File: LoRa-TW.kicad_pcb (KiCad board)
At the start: 2 copper layers, 4 parts, among them U1 SX1262IMLTRT

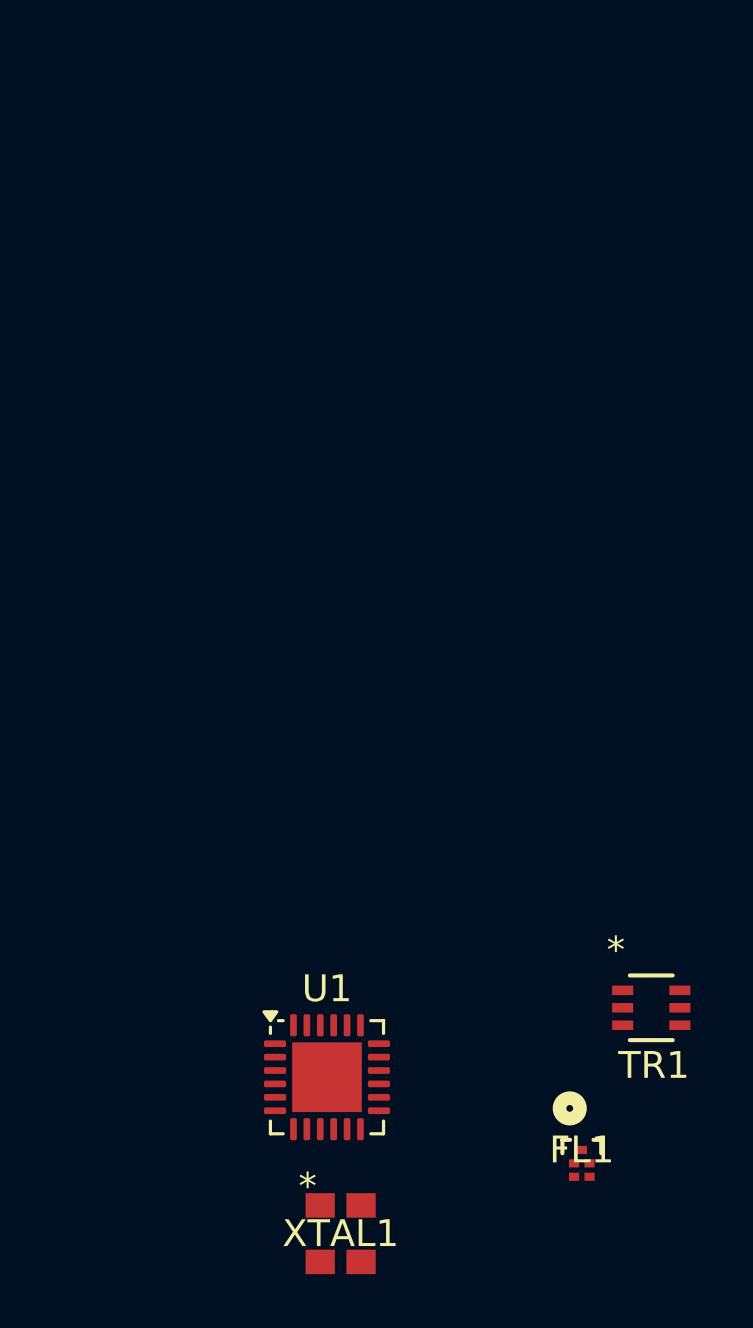
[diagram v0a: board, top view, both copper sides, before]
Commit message: update receive of schematic
- update symbol
- place rx path components
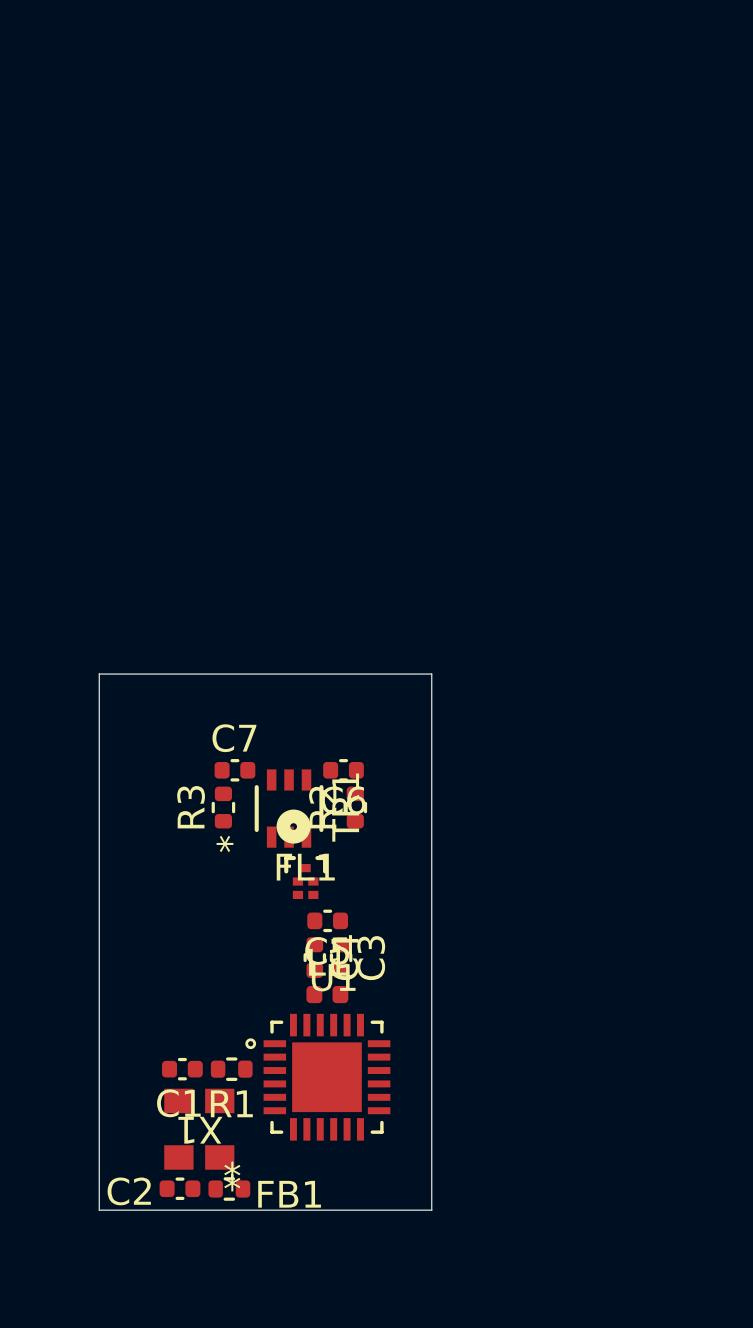
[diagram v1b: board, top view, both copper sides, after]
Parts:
- removed XTAL1: NT2016SA-32MHz-END4263A, LoRa-TW:NT2016SA_NDK
- added C1: 10P, Capacitor_SMD:C_0402_1005Metric, F.Cu at (149.4, 125.6)
- added C2: 100n, Capacitor_SMD:C_0402_1005Metric, F.Cu at (149.4, 130.0)
- added C3: 1p8, Capacitor_SMD:C_0402_1005Metric, F.Cu at (155.4, 121.4)
- added C4: 2p4, Capacitor_SMD:C_0402_1005Metric, F.Cu at (154.4, 121.4)
- added C5: 2p4, Capacitor_SMD:C_0402_1005Metric, F.Cu at (154.9, 120.0)
- added C6: 1n, Capacitor_SMD:C_0402_1005Metric, F.Cu at (155.5, 114.4)
- added C7: 1n, Capacitor_SMD:C_0402_1005Metric, F.Cu at (151.4, 114.4)
- added FB1: 100K, Resistor_SMD:R_0402_1005Metric, F.Cu at (151.2, 130.0)
- added L1: 15n, Inductor_SMD:L_0402_1005Metric, F.Cu at (154.9, 122.8)
- added R1: 220, Resistor_SMD:R_0402_1005Metric, F.Cu at (151.3, 125.6)
- added R2: 100, Resistor_SMD:R_0402_1005Metric, F.Cu at (155.9, 115.8)
- added R3: 100, Resistor_SMD:R_0402_1005Metric, F.Cu at (151.0, 115.8)
- added X1: TCXO, 32MHz, 2.0x1.6mm, LoRa-TW:NT2016SA_NDK, F.Cu at (150.1, 127.8)
- U1: footprint Package_DFN_QFN:QFN-24-1EP_4x4mm_P0.5mm_EP2.6x2.6mm -> LoRa-TW:SX1262IMLTRT
- moved TR1 15.4 mm to (153.4, 115.8), turned to 90 degrees
- moved FL1 14.7 mm to (154.0, 118.6)
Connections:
- FL1 pad 1: unconnected-(FL1-IN-Pad1) -> Net-(FL1-IN)
- FL1 pad 2: unconnected-(FL1-GND-Pad2) -> GND
- FL1 pad 3: unconnected-(FL1-GND-Pad3) -> GND
- FL1 pad 4: unconnected-(FL1-OUT-Pad4) -> Net-(FL1-OUT)
- FL1 pad 5: unconnected-(FL1-GND-Pad5) -> GND
- TR1 pad 3: unconnected-(TR1-RF2-Pad3) -> Net-(FL1-IN)
- TR1 pad 4: unconnected-(TR1-CTRL-Pad4) -> Net-(TR1-CTRL)
- TR1 pad 6: unconnected-(TR1-*CTRL/VDD-Pad6) -> Net-(TR1-~{CTRL}/VDD)
- U1 pad 12: unconnected-(U1-DIO2-Pad12) -> /DIO2
- U1 pad 15: unconnected-(U1-~{RESET}-Pad15) -> /~{RESET}
- U1 pad 21: unconnected-(U1-RFI_P-Pad21) -> Net-(U1-RFI_P)
- U1 pad 22: unconnected-(U1-RFI_N-Pad22) -> Net-(U1-RFI_N)
- U1 pad 3: unconnected-(U1-XTA-Pad3) -> /CLK_{32M}
- U1 pad 6: unconnected-(U1-DIO3-Pad6) -> /DIO3_CLK_{EN}
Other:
- board outline added: 12.4 x 20 mm

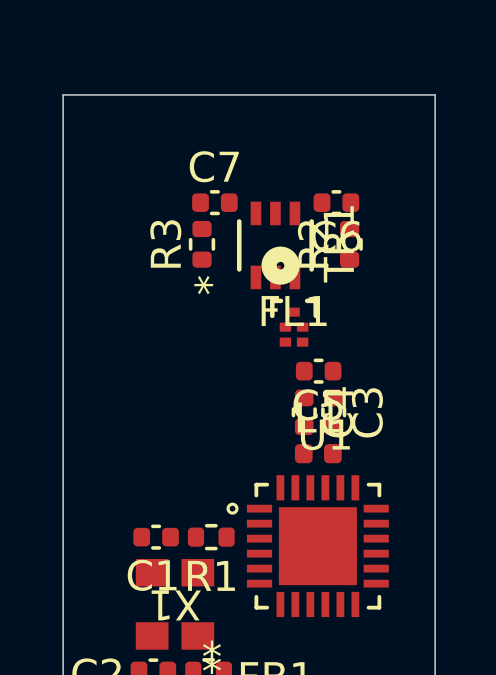
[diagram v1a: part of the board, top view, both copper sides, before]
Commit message: update transmit of schematic
- update TX path
- correct some components properties
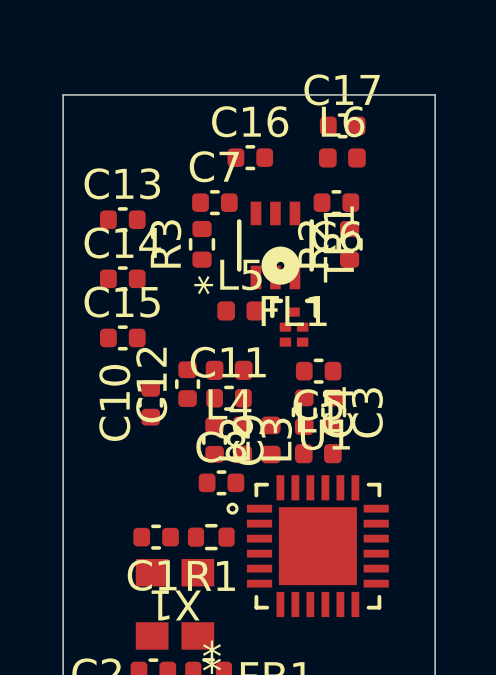
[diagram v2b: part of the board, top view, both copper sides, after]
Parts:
- added C10: 3p0, Capacitor_SMD:C_0402_1005Metric, F.Cu at (149.3, 121.1)
- added C11: 3p0, Capacitor_SMD:C_0402_1005Metric, F.Cu at (151.9, 120.9)
- added C12: 5p6, Capacitor_SMD:C_0402_1005Metric, F.Cu at (150.5, 120.5)
- added C13: 39p, Capacitor_SMD:C_0402_1005Metric, F.Cu at (148.3, 115.0)
- added C14: 1p8, Capacitor_SMD:C_0402_1005Metric, F.Cu at (148.3, 117.0)
- added C15: 39p, Capacitor_SMD:C_0402_1005Metric, F.Cu at (148.3, 118.9)
- added C16: 3p3, Capacitor_SMD:C_0402_1005Metric, F.Cu at (152.6, 112.9)
- added C17: 3p3, Capacitor_SMD:C_0402_1005Metric, F.Cu at (155.7, 111.8)
- added C8: 47n, Capacitor_SMD:C_0402_1005Metric, F.Cu at (151.6, 123.8)
- added C9: 47p, Capacitor_SMD:C_0402_1005Metric, F.Cu at (151.4, 122.3)
- added L2: 0, Inductor_SMD:L_0402_1005Metric, F.Cu at (153.3, 122.3)
- added L3: 47n, Inductor_SMD:L_0402_1005Metric, F.Cu at (152.3, 122.3)
- added L4: 2n5, Inductor_SMD:L_0402_1005Metric, F.Cu at (151.9, 120.0)
- added L5: 4n7, Inductor_SMD:L_0402_1005Metric, F.Cu at (152.3, 118.0)
- added L6: 9n1, Inductor_SMD:L_0402_1005Metric, F.Cu at (155.7, 112.9)
- FB1: value 100K -> 10R@100MHz
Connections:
- net /DIO2 renamed /DIO2_ANT_{SW}
- L1 pad 1: Net-(U1-RFI_N) -> Net-(U1-RFI_P)
- L1 pad 2: Net-(U1-RFI_P) -> Net-(U1-RFI_N)
- TR1 pad 1: unconnected-(TR1-RF1-Pad1) -> Net-(TR1-RF1)
- TR1 pad 2: unconnected-(TR1-GND-Pad2) -> GND
- TR1 pad 5: unconnected-(TR1-RFC-Pad5) -> Net-(TR1-RFC)
- U1 pad 13: unconnected-(U1-DIO1-Pad13) -> /DIO1_INT
- U1 pad 16: unconnected-(U1-MISO-Pad16) -> /SPI_MISO
- U1 pad 17: unconnected-(U1-MOSI-Pad17) -> /SPI_MOSI
- U1 pad 18: unconnected-(U1-SCK-Pad18) -> /SPI_CLK
- U1 pad 19: unconnected-(U1-NSS-Pad19) -> /SPI_NSS
- U1 pad 23: unconnected-(U1-RFO-Pad23) -> Net-(U1-RFO)
- U1 pad 24: unconnected-(U1-VR_PA-Pad24) -> Net-(U1-VR_PA)

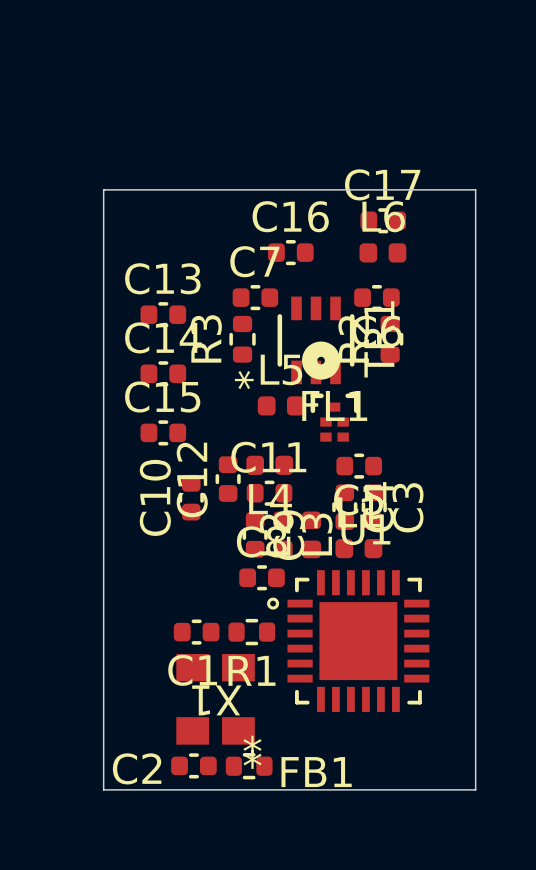
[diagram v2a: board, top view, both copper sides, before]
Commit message: update schematic for power input
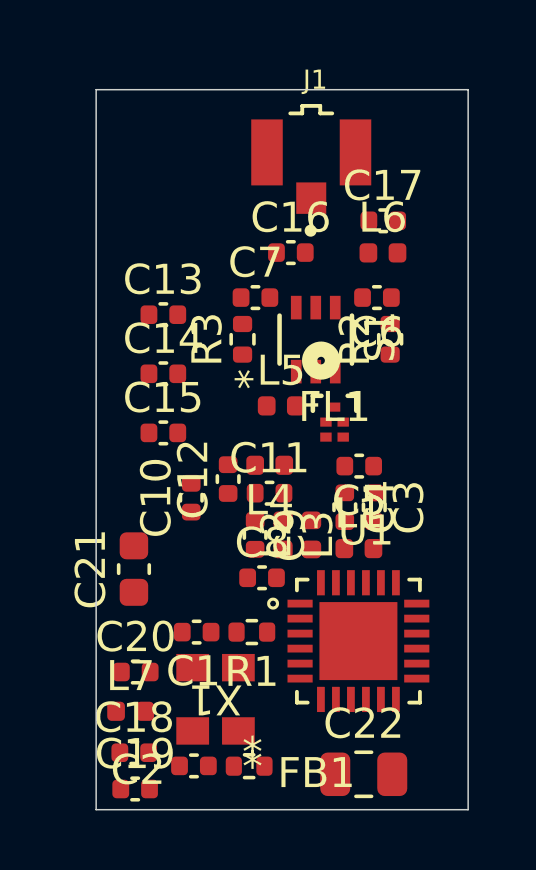
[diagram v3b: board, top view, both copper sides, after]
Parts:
- removed TR1: PE4259-63, LoRa-TW:SC-70-6_PSM
- added C18: 470n, Capacitor_SMD:C_0402_1005Metric, F.Cu at (147.4, 129.6)
- added C19: 100n, Capacitor_SMD:C_0402_1005Metric, F.Cu at (147.4, 130.8)
- added C20: 100n, Capacitor_SMD:C_0402_1005Metric, F.Cu at (147.4, 126.9)
- added C21: 1u, Capacitor_SMD:C_0603_1608Metric, F.Cu at (147.4, 123.5)
- added C22: 10u, Capacitor_SMD:C_0805_2012Metric, F.Cu at (155.0, 130.3)
- added J1: MHF-I/U.FL, LoRa-TW:IPEX_20279-001E-03, F.Cu at (153.3, 109.6)
- added L7: 15u, Inductor_SMD:L_0402_1005Metric, F.Cu at (147.2, 128.2)
- added S1: PE4259-63, LoRa-TW:SC-70-6_PSM, F.Cu at (153.4, 115.8)
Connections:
- U1 pad 1: unconnected-(U1-VDD_IN-Pad1) -> VDD
- U1 pad 10: unconnected-(U1-VBAT-Pad10) -> VDD
- U1 pad 11: unconnected-(U1-VBAT_IO-Pad11) -> VDD
- U1 pad 14: unconnected-(U1-BUSY-Pad14) -> /BUSY
- U1 pad 7: unconnected-(U1-VREG-Pad7) -> /VREG
- U1 pad 9: unconnected-(U1-DCC_SW-Pad9) -> Net-(U1-DCC_SW)
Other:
- board size 12.4 x 20 mm -> 12.4 x 24 mm

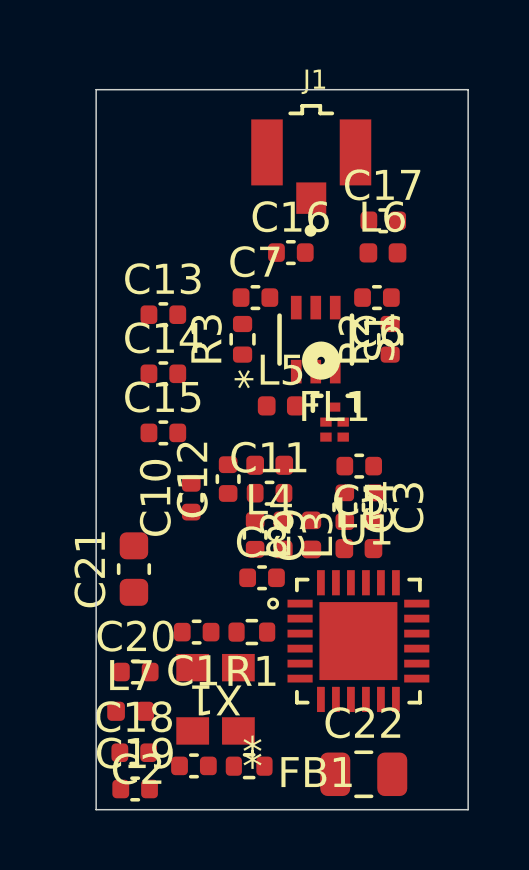
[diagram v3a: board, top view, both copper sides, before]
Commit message: update schematic & pcb for new footprint
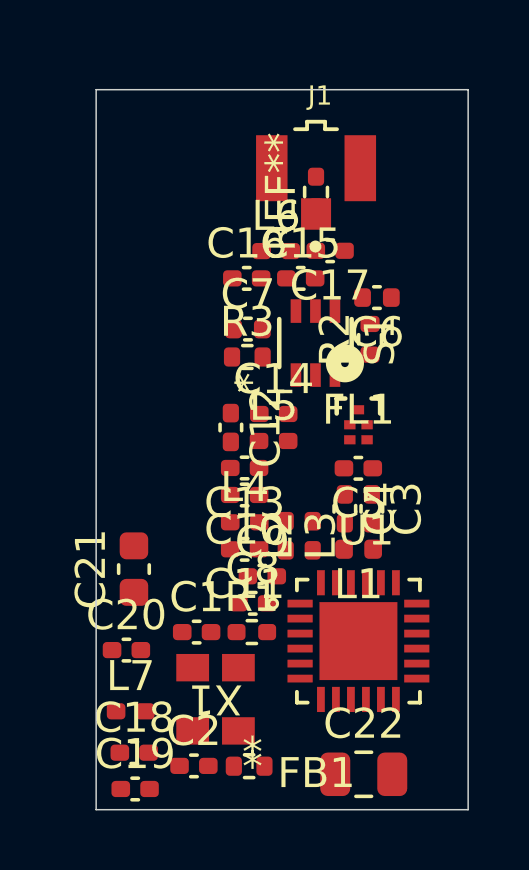
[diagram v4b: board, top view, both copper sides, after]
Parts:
- added REF**: R_HF_0402_1005Metric, LoRa-TW:R_HF_0402_1005Metric, F.Cu at (153.4, 110.9)
- C1, C10, C11, C12, C13, C14, C15, C16, C17, C18, C19, C2, C20, C3, C4, C5, C8, C9: footprint Capacitor_SMD:C_0402_1005Metric -> LoRa-TW:C_HF_0402_1005Metric
- L2, L3, L4, L5, L6, L7: footprint Inductor_SMD:L_0402_1005Metric -> LoRa-TW:L_HF_0402_1005Metric
- R1: footprint Resistor_SMD:R_0402_1005Metric -> LoRa-TW:R_HF_0402_1005Metric
- moved C15 6.89 mm to (152.9, 113.8)
- moved C13 5.78 mm to (151.1, 120.1), turned to 180 degrees
- moved C14 3.92 mm to (152.0, 118.3)
- moved L6 3.56 mm to (152.1, 112.9)
- moved L4 2.07 mm to (151.1, 121.9), turned to 0 degrees
- moved C11 2.05 mm to (151.1, 122.8), turned to 180 degrees
- moved C17 2.03 mm to (153.9, 112.8), turned to 180 degrees
- moved C10 1.78 mm to (151.1, 121.0), turned to 180 degrees
- moved C12 1.72 mm to (150.6, 118.7), turned to -90 degrees
- moved C16 1.70 mm to (151.1, 113.8)
- moved C9 1.40 mm to (151.6, 123.7), turned to 0 degrees
- moved L5 1.20 mm to (152.0, 119.2)
- moved C7 1.08 mm to (151.2, 115.5)
- moved C8 0.90 mm to (151.3, 124.6)
- moved FL1 0.80 mm to (154.8, 118.7)
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
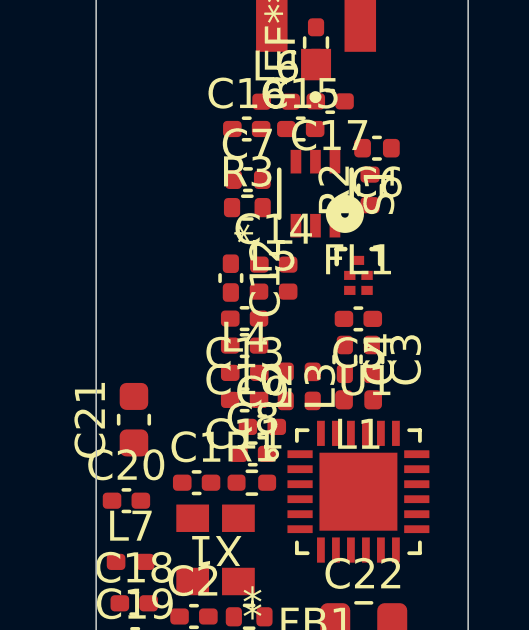
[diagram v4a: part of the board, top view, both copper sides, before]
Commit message: update SAW Filter properties with 3D Model
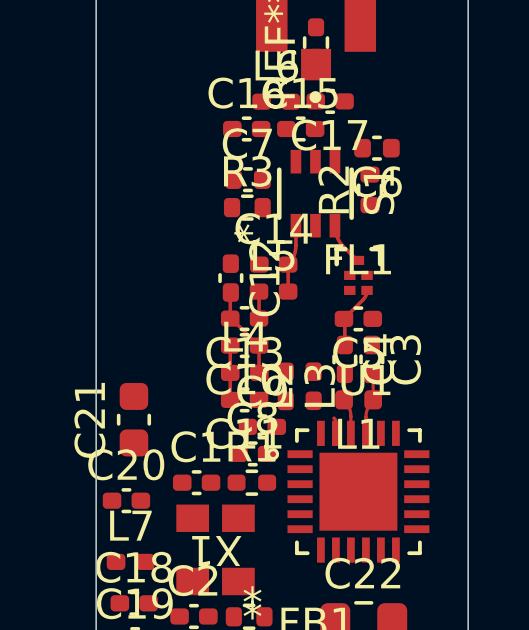
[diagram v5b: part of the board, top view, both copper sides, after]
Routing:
- net Net-(C10-Pad1): track 0.00 -> 3.14 mm
- net Net-(S1-RF1): track 0.00 -> 2.26 mm
- net Net-(FL1-OUT): track 0.00 -> 2.13 mm
- net Net-(U1-RFI_P): track 0.00 -> 2.06 mm
- net Net-(U1-RFI_N): track 0.00 -> 2.05 mm
- net Net-(C10-Pad2): track 0.00 -> 1.81 mm
- net Net-(FL1-IN): track 0.00 -> 1.45 mm
- net Net-(C13-Pad1): track 0.00 -> 0.90 mm
- net Net-(U1-RFO): track 0.00 -> 0.58 mm
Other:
- copper layers 2 -> 4

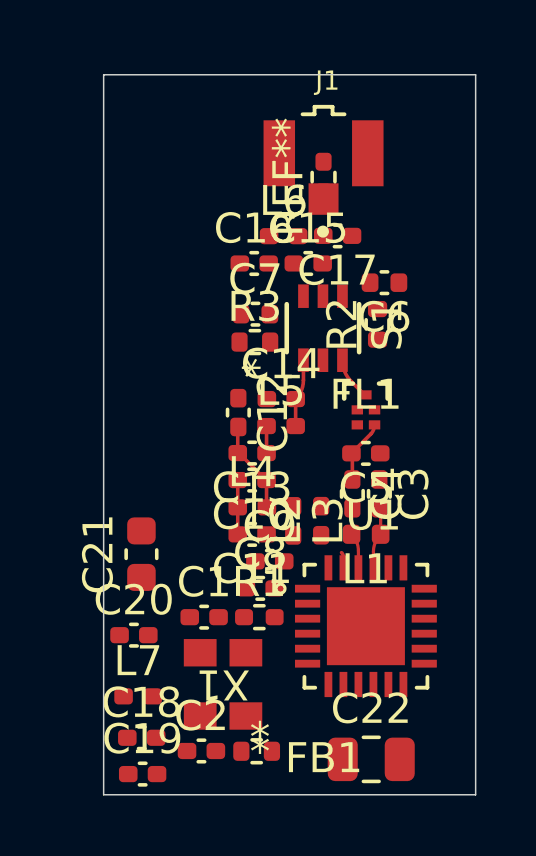
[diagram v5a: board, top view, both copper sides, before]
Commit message: update layout for RF parts
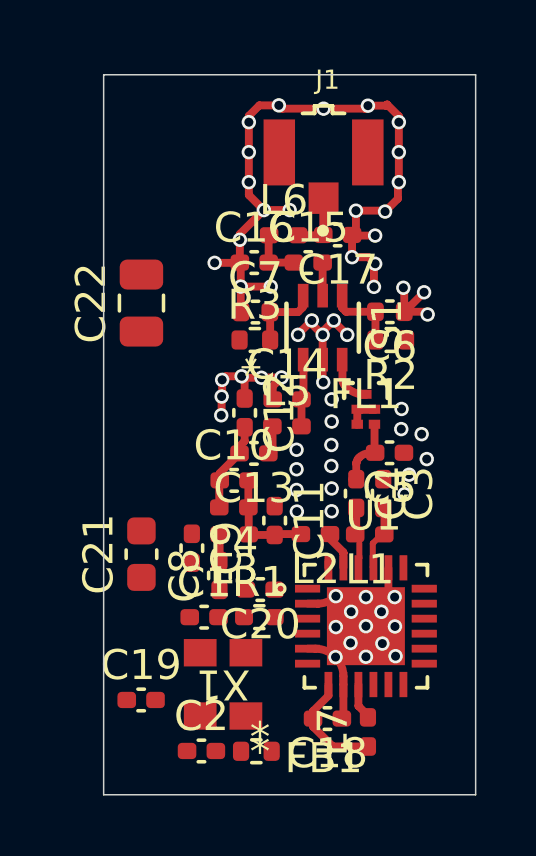
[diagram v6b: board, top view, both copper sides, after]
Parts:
- removed REF**: R_HF_0402_1005Metric, LoRa-TW:R_HF_0402_1005Metric
- L1: footprint Inductor_SMD:L_0402_1005Metric -> LoRa-TW:L_HF_0402_1005Metric
- moved C22 17.0 mm to (147.4, 115.1), turned to 90 degrees
- moved L7 7.75 mm to (154.9, 129.4), turned to 90 degrees
- moved C18 6.22 mm to (153.6, 128.9), turned to 180 degrees
- moved C20 4.48 mm to (151.3, 124.6), turned to 180 degrees
- moved C9 2.64 mm to (149.0, 123.3), turned to -90 degrees
- moved C19 2.47 mm to (147.3, 128.3)
- moved L3 2.02 mm to (150.4, 122.8), turned to 180 degrees
- moved C8 1.43 mm to (150.0, 124.2), turned to 90 degrees
- moved C6 0.99 mm to (155.6, 115.4)
- moved C11 0.88 mm to (151.8, 122.3), turned to -90 degrees
- moved C5 0.79 mm to (155.6, 120.1)
- moved R2 0.68 mm to (155.7, 116.3), turned to 180 degrees
- moved L4 0.62 mm to (150.4, 121.9), turned to 180 degrees
- moved C10 0.60 mm to (150.4, 121.0), turned to 0 degrees
- moved L2 0.48 mm to (153.2, 122.8), turned to 180 degrees
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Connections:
- net Net-(U1-RFI_N) renamed /RFI_N
- net Net-(U1-RFI_P) renamed /RFI_P
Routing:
- net GND: track 0.00 -> 41.5 mm, vias 0 -> 65
- net /VREG: track 0.00 -> 3.74 mm
- net Net-(S1-CTRL): track 0.00 -> 2.51 mm
- net Net-(S1-~{CTRL}/VDD): track 0.00 -> 2.50 mm
- net Net-(C17-Pad2): track 0.00 -> 2.07 mm
- net Net-(C10-Pad2): track 1.81 -> 3.61 mm
- net Net-(C15-Pad1): track 0.00 -> 1.75 mm
- net Net-(U1-DCC_SW): track 0.00 -> 1.23 mm
- net Net-(U1-VR_PA): track 0.00 -> 1.13 mm
- net Net-(S1-RFC): track 0.00 -> 1.10 mm
- net Net-(U1-RFO): track 0.58 -> 1.41 mm
